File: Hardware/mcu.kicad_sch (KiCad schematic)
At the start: 0 parts

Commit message: feat(mcu): finalize core schematic and update project documentation
- MCU_Core: Completed pin definitions and Hierarchical Labels (SPI, UART, I2C, Motors).
- Root: Updated sheet pins to reflect the new MCU architecture.
- Docs: Refined README.md with detailed hierarchical roadmap and MIT License.
- Docs: Added 'Connectors & I/O' breakdown to the development plan.
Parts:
- added C10, C11, C12, C13, C17, C20, C9: 100nF 16V, symbol Device:C
- added C14, C18, C19: 4.7uF 16V, symbol Device:C
- added C15, C16: 22pF 16V, symbol Device:C
- added C21: 1uF 16V, symbol Device:C
- added FB1: FerriteBead, symbol Device:FerriteBead
- added R5, R6: 10k, symbol Device:R
- added SW1, SW2: SW_Push, symbol Switch:SW_Push
- added U4: STM32F405RGT6, Package_QFP:LQFP-64_10x10mm_P0.5mm, symbol MCU_ST_STM32F4:STM32F405RGTx
- added Y1: Crystal_GND24, symbol Device:Crystal_GND24
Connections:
- new net: C20.2, C21.2, FB1.1, U4.13 (VDDA)
- new net: C17.2, R5.2, SW1.2, U4.7 (NRST)
- new net: R6.2, SW2.1, U4.60 (BOOT0)
- new net: C15.2, U4.5 (PH0), Y1.1
- new net: C16.2, U4.6 (PH1), Y1.3
- new net: C19.2, U4.47 (VCAP_2)
- new net: C18.2, U4.31 (VCAP_1)
- new net +3.3V: C10.1, C11.1, C12.1, C13.1, C14.1, C9.1, FB1.2, R5.1, SW2.2, U4.1 (VBAT), U4.19 (VDD), U4.32 (VDD), U4.48 (VDD), U4.64 (VDD)
- new net CURRENT_SENSE: U4.9 (PC1)
- new net GND: C10.2, C11.2, C12.2, C13.2, C14.2, C15.1, C16.1, C17.1, C18.1, C19.1, C20.1, C21.1, C9.2, R6.1, SW1.1, U4.12 (VSSA), U4.18 (VSS), U4.63 (VSS), Y1.2 (G), Y1.4 (G)
- new net GYRO_CS: U4.20 (PA4)
- new net I2C1_SCL: U4.58 (PB6)
- new net I2C1_SDA: U4.59 (PB7)
- new net MOTOR_1: U4.26 (PB0)
- new net MOTOR_2: U4.27 (PB1)
- new net MOTOR_3: U4.56 (PB4)
- new net MOTOR_4: U4.57 (PB5)
- new net OSD_CS: U4.33 (PB12)
- new net RX1: U4.43 (PA10)
- new net RX3: U4.30 (PB11)
- new net RX4: U4.15 (PA1)
- new net RX6: U4.38 (PC7)
- new net SPI1_MISO: U4.23 (PA7)
- new net SPI1_MOSI: U4.22 (PA6)
- new net SPI1_SCK: U4.21 (PA5)
- new net SPI2_MISO: U4.35 (PB14)
- new net SPI2_MOSI: U4.36 (PB15)
- new net SPI2_SCK: U4.34 (PB13)
- new net TX1: U4.42 (PA9)
- new net TX3: U4.29 (PB10)
- new net TX4: U4.14 (PA0)
- new net TX6: U4.37 (PC6)
- new net USB_DM: U4.44 (PA11)
- new net USB_DP: U4.45 (PA12)
- new net VBAT_SENSE: U4.8 (PC0)

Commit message: feat: implement system peripherals (OSD, Gyro, Baro)
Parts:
- FB1: value FerriteBead -> 100R @ 100MHz
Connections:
- net GYRO_EXTI: now reaches U4.24 (PC4)
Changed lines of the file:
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@@
+	(wire
+		(pts
+			(xy 106.68 86.36) (xy 110.49 86.36)
+		)
+		(stroke
+			(width 0)
+			(type default)
+		)
+	)
 	(wire
 		(pts
@@
 		)
 	)
+	(hierarchical_label "GYRO_EXTI"
+		(shape input)
+		(at 106.68 86.36 180)
+		(effects
+			(font
+				(size 1.27 1.27)
+			)
+			(justify right)
+		)
+	)
 	(hierarchical_label "MOTOR_1"
 		(shape output)
@@
 	)
 	(hierarchical_label "I2C1_SCL"
-		(shape output)
+		(shape bidirectional)
 		(at 154.94 111.76 0)
 		(effects
@@
 			)
 		)
-		(property "Value" "FerriteBead"
+		(property "Value" "100R @ 100MHz"
 			(at 153.6192 34.29 90)
 			(effects

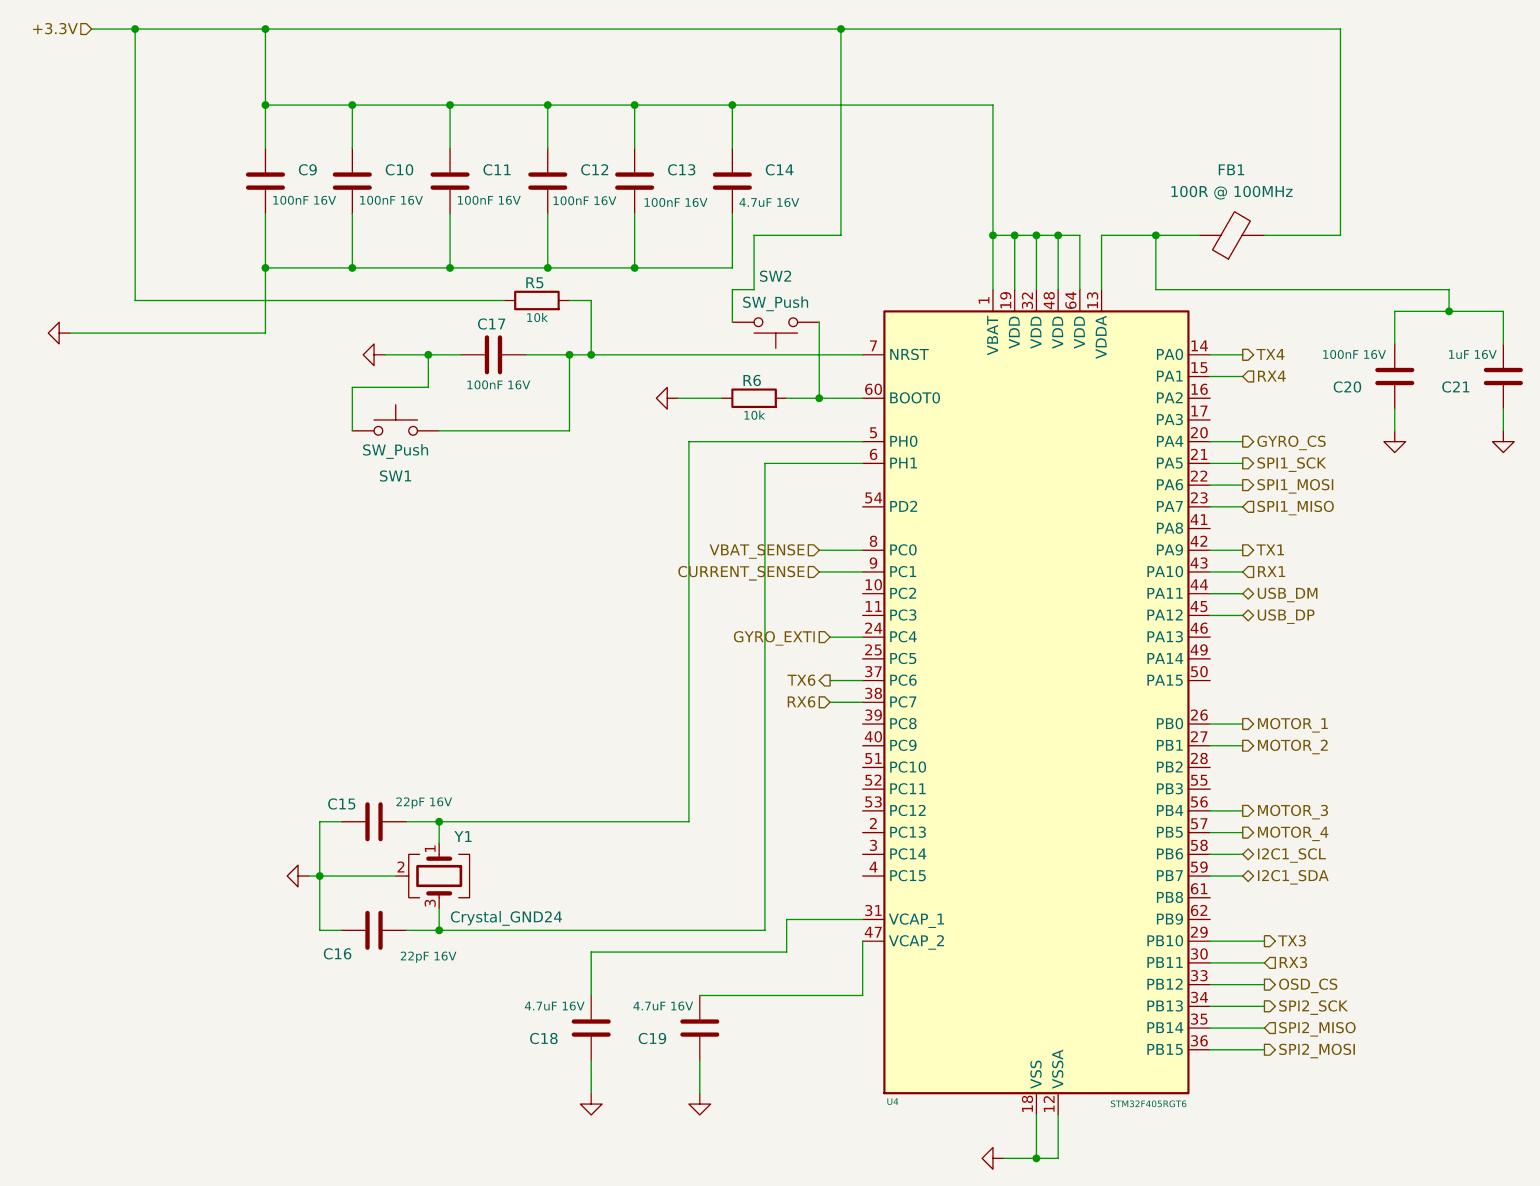
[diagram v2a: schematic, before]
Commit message: Finalize schematic: Add connectors, LEDs, Buzzer and fix all ERC errors
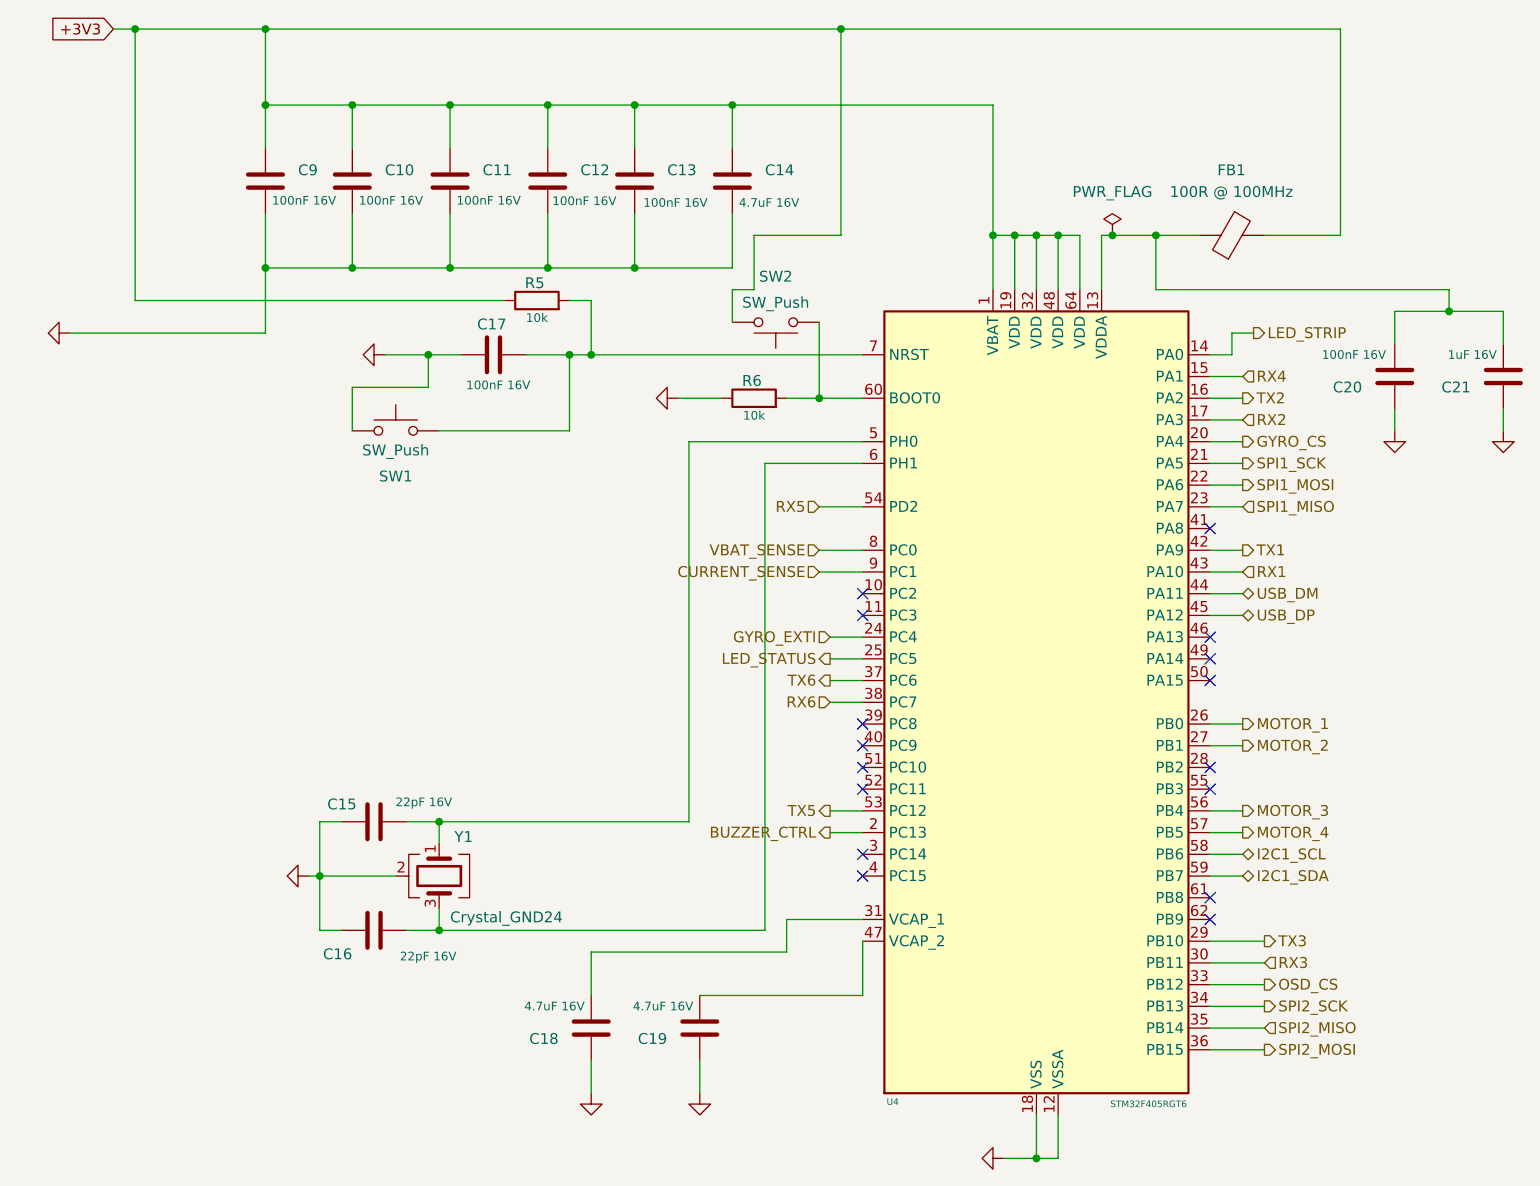
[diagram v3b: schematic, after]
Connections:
- net TX2: now reaches U4.16 (PA2)
- net RX2: now reaches U4.17 (PA3)
- net BUZZER_CTRL: now reaches U4.2 (PC13)
- net LED_STATUS: now reaches U4.25 (PC5)
- net TX5: now reaches U4.53 (PC12)
- net RX5: now reaches U4.54 (PD2)
- net +3.3V renamed +3V3
- net TX4 renamed LED_STRIP
- no-connect marks 0 -> 16

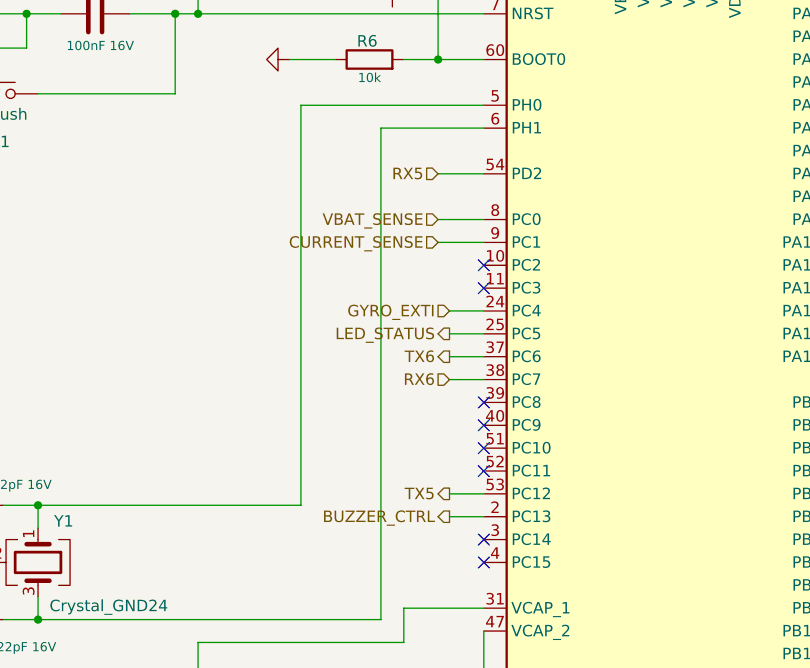
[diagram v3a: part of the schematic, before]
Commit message: Update schematic: Add SDIO Blackbox, ESC Redundancy and remove UART5
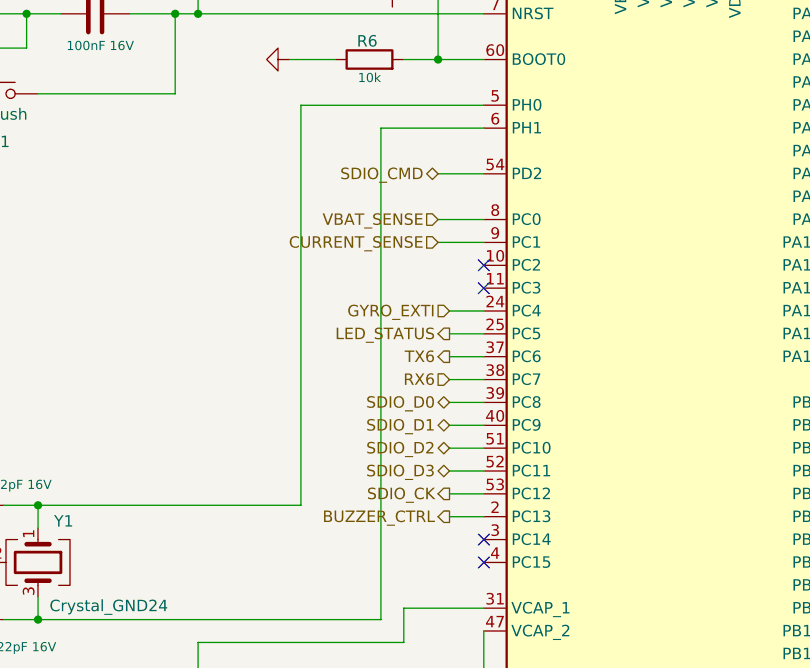
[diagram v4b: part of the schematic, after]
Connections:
- net SDIO_D0: now reaches U4.39 (PC8)
- net SDIO_D1: now reaches U4.40 (PC9)
- net SDIO_D2: now reaches U4.51 (PC10)
- net SDIO_D3: now reaches U4.52 (PC11)
- net RX5 renamed SDIO_CMD
- net TX5 renamed SDIO_CK
- no-connect marks 16 -> 12

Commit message: Finalize component placement and silkscreen
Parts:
- C10, C11, C12, C13, C14, C15, C16, C17, C18, C19, C20, C21, C9: footprint (none) -> Capacitor_SMD:C_0402_1005Metric
- FB1: footprint (none) -> Inductor_SMD:L_0402_1005Metric
- R5, R6: footprint (none) -> Resistor_SMD:R_0402_1005Metric
- SW1, SW2: footprint (none) -> Button_Switch_SMD:SW_Push_1P1T_NO_CK_KMR2
- Y1: footprint (none) -> Crystal:Crystal_SMD_3225-4Pin_3.2x2.5mm
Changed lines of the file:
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@@
 			)
 		)
-		(property "Footprint" ""
+		(property "Footprint" "Inductor_SMD:L_0402_1005Metric"
 			(at 153.67 41.148 90)
 			(effects
@@
 			)
 		)
-		(property "Footprint" ""
+		(property "Footprint" "Capacitor_SMD:C_0402_1005Metric"
 			(at 71.12 52.3748 0)
 			(effects
@@
 			)
 		)
-		(property "Footprint" ""
+		(property "Footprint" "Capacitor_SMD:C_0402_1005Metric"
 			(at 41.6052 36.83 0)
 			(effects
@@
 			)
 		)
-		(property "Footprint" ""
+		(property "Footprint" "Button_Switch_SMD:SW_Push_1P1T_NO_CK_KMR2"
 			(at 55.88 57.15 0)
 			(effects
@@
 			)
 		)
-		(property "Footprint" ""
+		(property "Footprint" "Button_Switch_SMD:SW_Push_1P1T_NO_CK_KMR2"
 			(at 100.33 54.61 0)
 			(effects
@@
 			)
 		)
-		(property "Footprint" ""
+		(property "Footprint" "Capacitor_SMD:C_0402_1005Metric"
 			(at 184.4548 52.07 0)
 			(effects
@@
 			)
 		)
-		(property "Footprint" ""
+		(property "Footprint" "Crystal:Crystal_SMD_3225-4Pin_3.2x2.5mm"
 			(at 60.96 114.3 0)
 			(effects
@@
 			)
 		)
-		(property "Footprint" ""
+		(property "Footprint" "Capacitor_SMD:C_0402_1005Metric"
 			(at 90.4748 128.27 0)
 			(effects
@@
 			)
 		)
-		(property "Footprint" ""
+		(property "Footprint" "Capacitor_SMD:C_0402_1005Metric"
 			(at 74.6252 36.83 0)
 			(effects
@@
 			)
 		)
-		(property "Footprint" ""
+		(property "Footprint" "Resistor_SMD:R_0402_1005Metric"
 			(at 97.79 60.198 90)
 			(effects
@@
 			)
 		)
-		(property "Footprint" ""
+		(property "Footprint" "Capacitor_SMD:C_0402_1005Metric"
 			(at 84.7852 36.83 0)
 			(effects
@@
 			)
 		)
-		(property "Footprint" ""
+		(property "Footprint" "Capacitor_SMD:C_0402_1005Metric"
 			(at 96.2152 36.83 0)
 			(effects
@@
 			)
 		)
-		(property "Footprint" ""
+		(property "Footprint" "Capacitor_SMD:C_0402_1005Metric"
 			(at 171.7548 52.07 0)
 			(effects
@@
 			)
 		)
-		(property "Footprint" ""
+		(property "Footprint" "Capacitor_SMD:C_0402_1005Metric"
 			(at 57.15 119.6848 0)
 			(effects
@@
 			)
 		)
-		(property "Footprint" ""
+		(property "Footprint" "Capacitor_SMD:C_0402_1005Metric"
 			(at 57.15 106.9848 0)
 			(effects
@@
 			)
 		)
-		(property "Footprint" ""
+		(property "Footprint" "Capacitor_SMD:C_0402_1005Metric"
 			(at 63.1952 36.83 0)
 			(effects
@@
 			)
 		)
-		(property "Footprint" ""
+		(property "Footprint" "Capacitor_SMD:C_0402_1005Metric"
 			(at 51.7652 36.83 0)
 			(effects
@@
 			)
 		)
-		(property "Footprint" ""
+		(property "Footprint" "Resistor_SMD:R_0402_1005Metric"
 			(at 72.39 48.768 90)
 			(effects
@@
 			)
 		)
-		(property "Footprint" ""
+		(property "Footprint" "Capacitor_SMD:C_0402_1005Metric"
 			(at 77.7748 128.27 0)
 			(effects
